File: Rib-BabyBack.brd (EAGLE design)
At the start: 67.3 x 74.9 mm, 30 parts, among them IC1 REG1117, SW1 DPDT

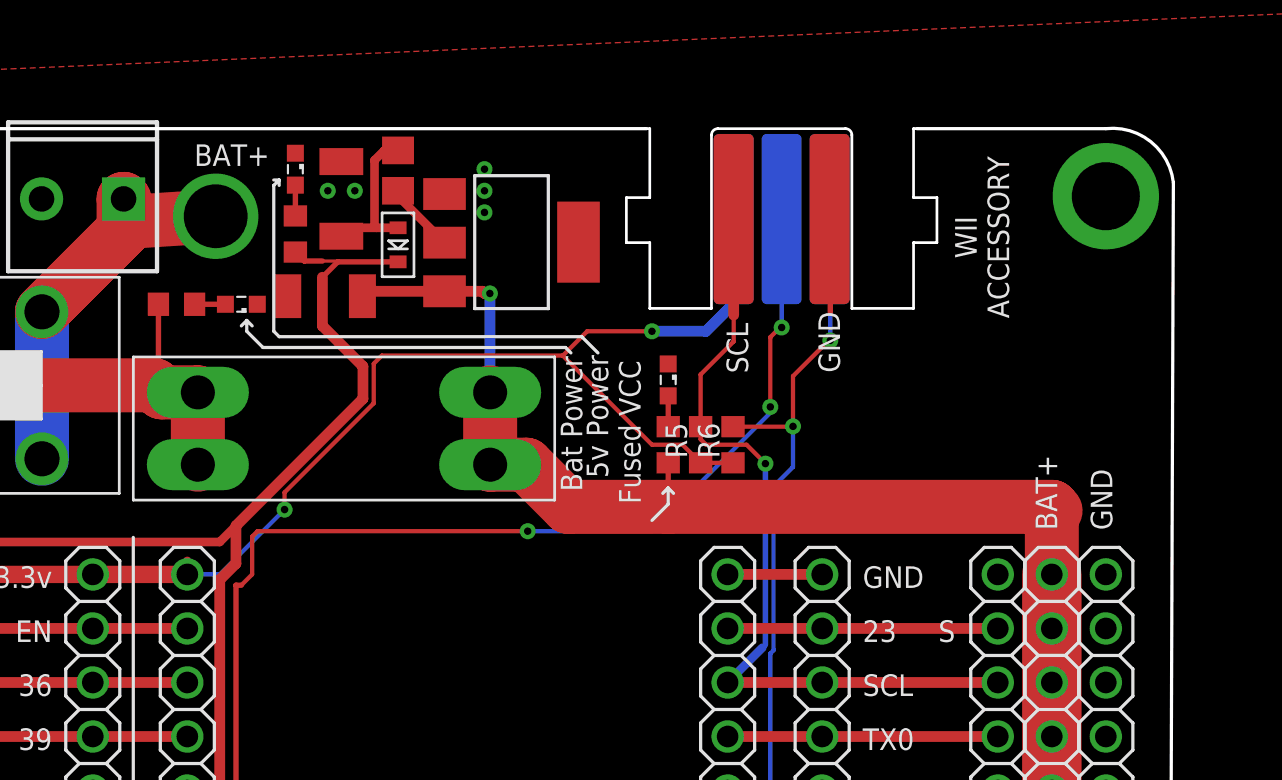
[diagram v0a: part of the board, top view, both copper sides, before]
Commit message: Moved fuse holder as per #40
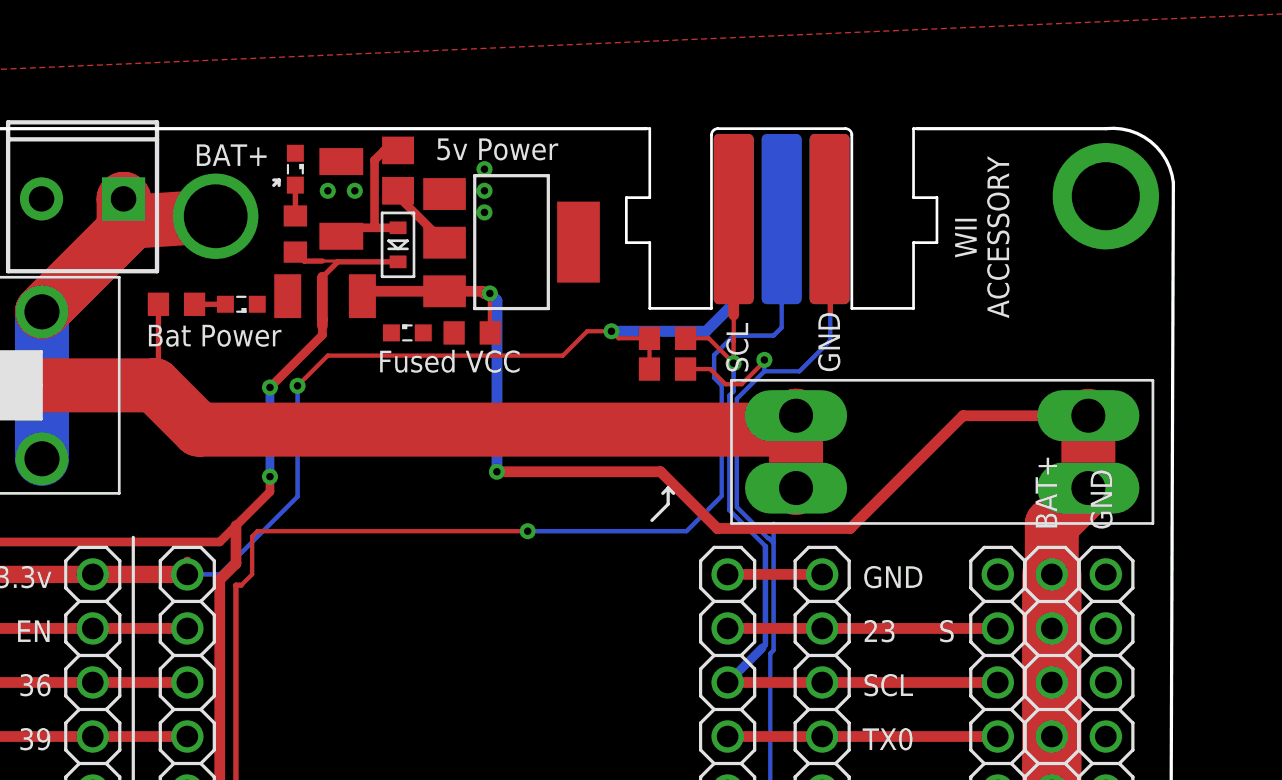
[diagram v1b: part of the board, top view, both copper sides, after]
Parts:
- moved F4 28.1 mm to (56.8, 60.4)
- moved LED1 12.5 mm to (31.7, 66.0), turned to 0 degrees
- moved R1 10.6 mm to (34.7, 66.0), turned to 0 degrees
- moved R5 5.24 mm to (43.9, 65.7), turned to 0 degrees
- moved R6 4.70 mm to (43.9, 64.3), turned to 0 degrees
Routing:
- net LIPORAW: track 35.5 -> 64.6 mm
- net VCC: track 139.9 -> 147.5 mm, vias 1 -> 2
- net SDA: track 45.6 -> 51.1 mm, vias 3 -> 2
- net 3V3: track 135.2 -> 130.0 mm
- net DET: track 77.1 -> 79.4 mm, vias 4 -> 2
- net N$24: track 1.45 -> 0.00 mm
- net 5V: track 117.4 -> 116.1 mm, vias 2 -> 4
- net SCL: track 34.2 -> 34.7 mm

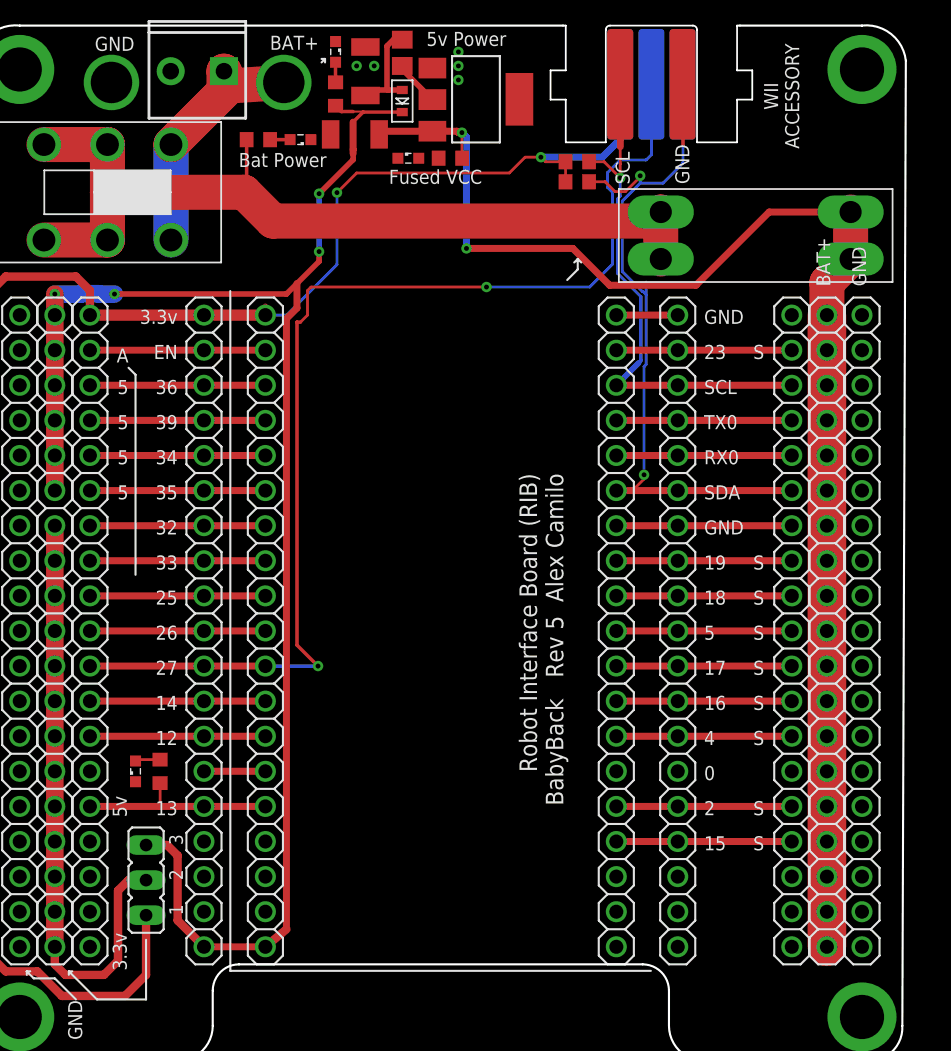
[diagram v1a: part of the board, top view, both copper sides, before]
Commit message: Updated silkscreen indicating analog pins #41
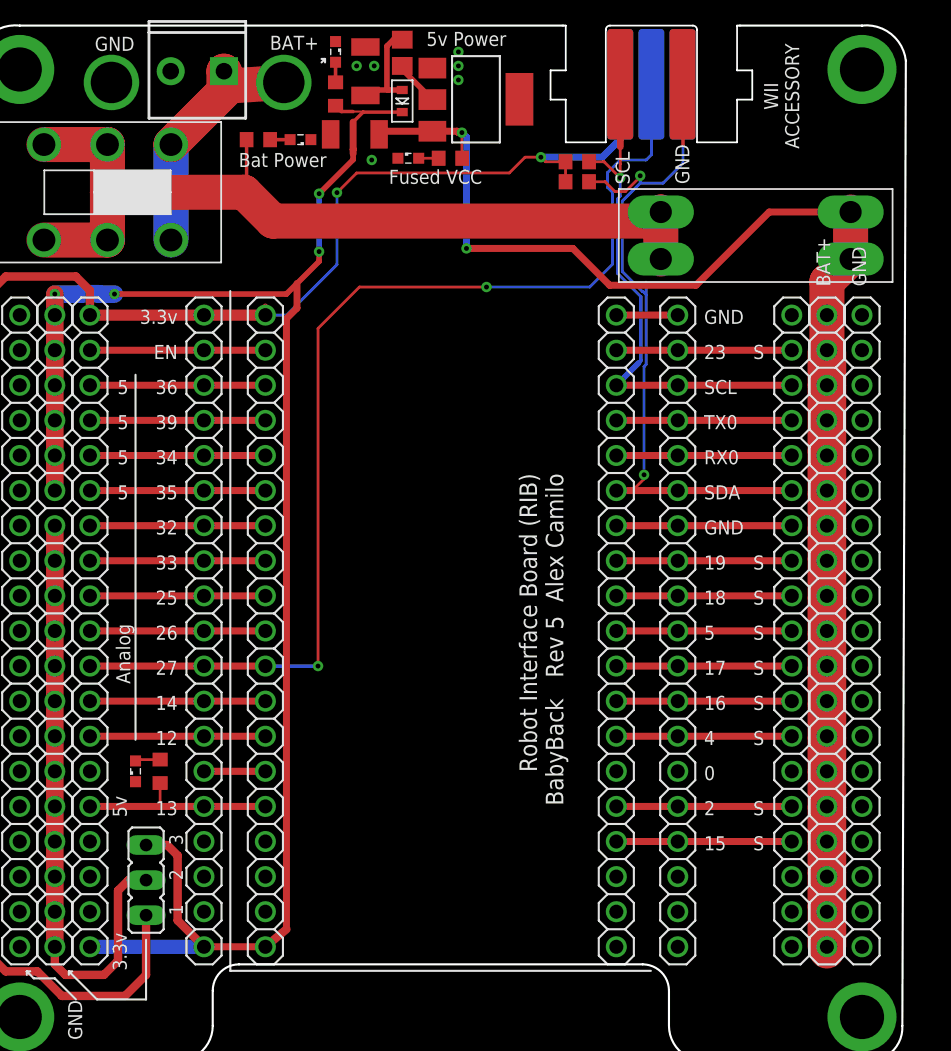
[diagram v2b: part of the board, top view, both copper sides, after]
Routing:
- net 5V: track 116.1 -> 124.4 mm
- net SDA: track 51.1 -> 55.0 mm
- net N$24: track 0.00 -> 1.45 mm
- net VCC: track 147.5 -> 146.1 mm
- net DET: track 79.4 -> 80.1 mm
- net GND: vias 10 -> 11
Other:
- board text added: "Analog"
- board text removed: "A"

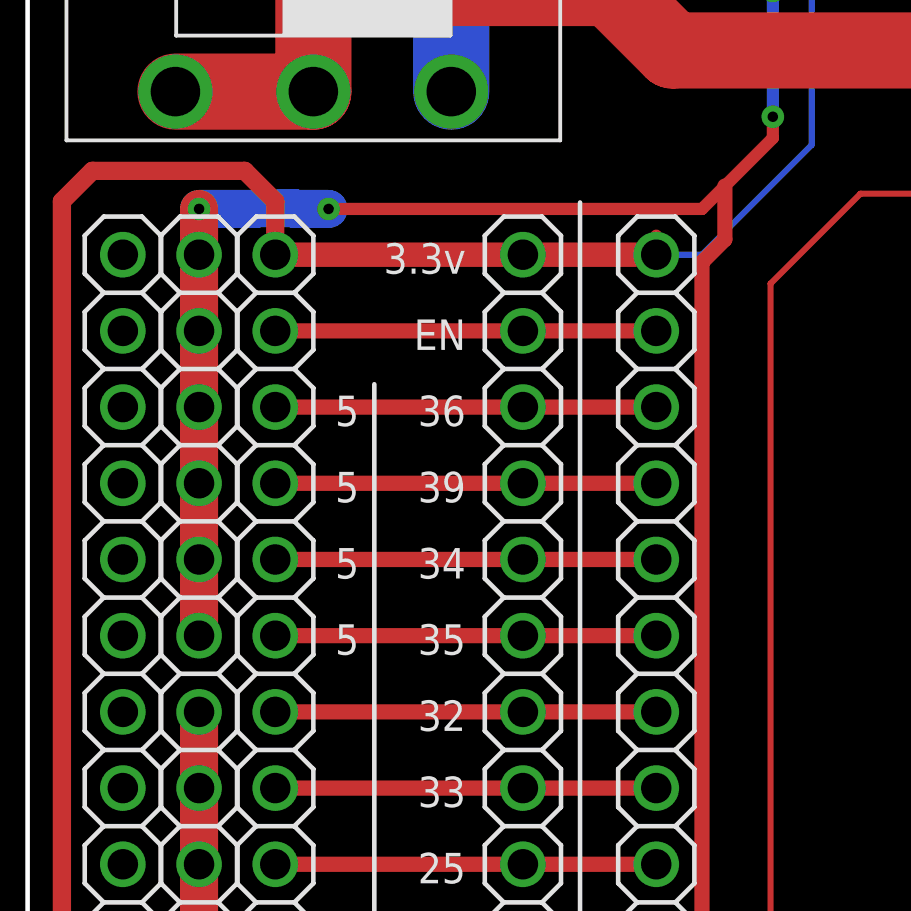
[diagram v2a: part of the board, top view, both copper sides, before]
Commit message: changed 5v rail
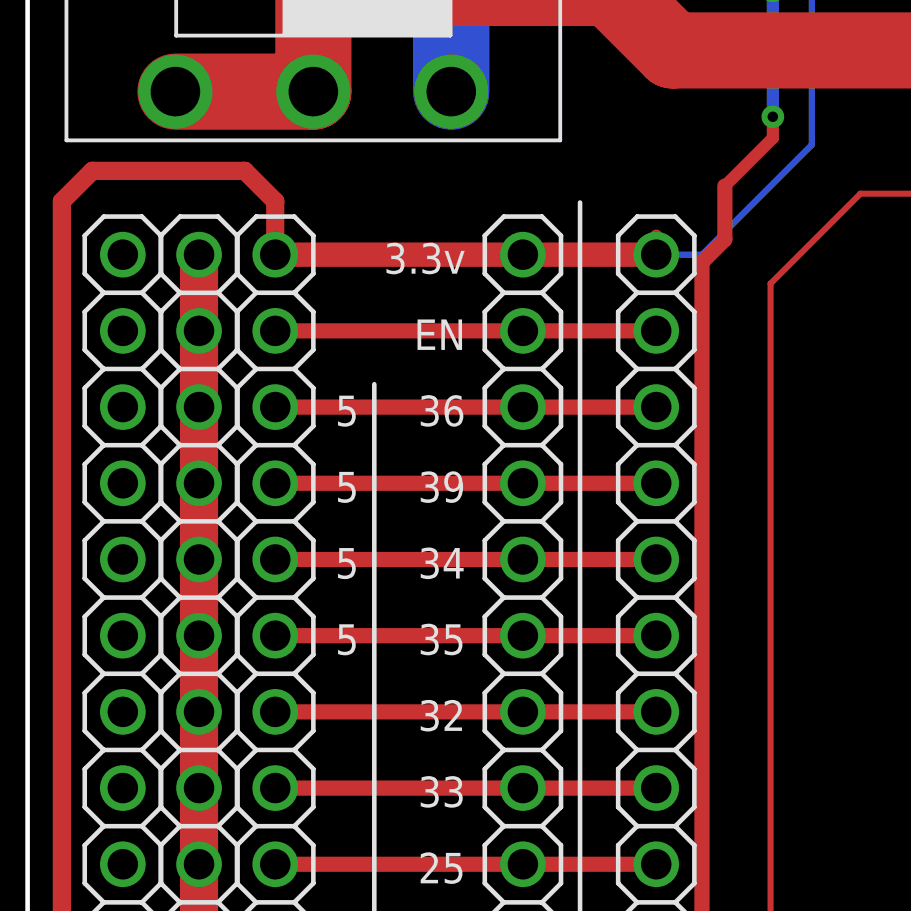
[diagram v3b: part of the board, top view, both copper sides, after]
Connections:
- net 5V: no longer JP4.14, JP4.15, JP4.16, JP4.17, JP4.18, JP4.19
- net SENSORV: now also JP4.14, JP4.15, JP4.16, JP4.17, JP4.18, JP4.19
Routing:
- net 5V: track 124.4 -> 92.3 mm, vias 4 -> 2
- net SENSORV: track 44.5 -> 59.7 mm
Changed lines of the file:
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@@
 <?xml version="1.0" encoding="utf-8"?>
 <!DOCTYPE eagle SYSTEM "eagle.dtd">
-<eagle version="8.6.3">
+<eagle version="9.1.0">
 <drawing>
 <settings>
@@
 <param name="checkStop" value="0"/>
 <param name="checkValues" value="0"/>
+<param name="checkNames" value="1"/>
+<param name="checkWireStubs" value="1"/>
+<param name="checkPolygonWidth" value="0"/>
 <param name="useDiameter" value="13"/>
 <param name="maxErrors" value="50"/>
@@
 <wire x1="31.242" y1="69.304" x2="28.41" y2="69.304" width="0.254" layer="1"/>
 <wire x1="28.41" y1="69.304" x2="27.686" y2="68.58" width="0.254" layer="1"/>
-<contactref element="JP4" pad="15"/>
-<contactref element="JP4" pad="19"/>
-<contactref element="JP4" pad="16"/>
-<contactref element="JP4" pad="17"/>
-<contactref element="JP4" pad="18"/>
-<contactref element="JP4" pad="14"/>
-<wire x1="6.096" y1="41.91" x2="6.096" y2="44.45" width="1.27" layer="1"/>
-<wire x1="6.096" y1="44.45" x2="6.096" y2="46.99" width="1.27" layer="1"/>
-<wire x1="6.096" y1="46.99" x2="6.096" y2="49.53" width="1.27" layer="1"/>
-<wire x1="6.096" y1="49.53" x2="6.096" y2="52.07" width="1.27" layer="1"/>
-<wire x1="6.096" y1="52.07" x2="6.096" y2="54.61" width="1.27" layer="1"/>
-<wire x1="6.096" y1="54.61" x2="6.096" y2="56.134" width="1.27" layer="1"/>
-<via x="6.096" y="56.134" extent="1-16" drill="0.35"/>
-<via x="10.414" y="56.134" extent="1-16" drill="0.35"/>
-<wire x1="6.096" y1="56.134" x2="7.9688125" y2="56.134" width="1.27" layer="16"/>
-<wire x1="7.9688125" y1="56.134" x2="7.9942125" y2="56.1594" width="1.27" layer="16"/>
-<wire x1="7.9942125" y1="56.1594" x2="9.2777875" y2="56.1594" width="1.27" layer="16"/>
-<wire x1="9.2777875" y1="56.1594" x2="9.3031875" y2="56.134" width="1.27" layer="16"/>
-<wire x1="9.3031875" y1="56.134" x2="10.414" y2="56.134" width="1.27" layer="16"/>
-<wire x1="10.414" y1="56.134" x2="22.86" y2="56.134" width="0.4064" layer="1"/>
-<wire x1="22.86" y1="56.134" x2="23.622" y2="56.896" width="0.4064" layer="1"/>
 <wire x1="28.41" y1="69.304" x2="28.372" y2="69.342" width="0.1524" layer="1"/>
 <wire x1="28.372" y1="69.342" x2="26.836" y2="69.342" width="0.1524" layer="1"/>
@@
 <wire x1="6.096" y1="34.29" x2="6.096" y2="36.83" width="1.27" layer="1"/>
 <wire x1="6.096" y1="36.83" x2="6.096" y2="39.37" width="1.27" layer="1"/>
+<contactref element="JP4" pad="15"/>
+<contactref element="JP4" pad="19"/>
+<contactref element="JP4" pad="16"/>
+<contactref element="JP4" pad="17"/>
+<contactref element="JP4" pad="18"/>
+<contactref element="JP4" pad="14"/>
+<wire x1="6.096" y1="44.45" x2="6.096" y2="46.99" width="1.27" layer="1"/>
+<wire x1="6.096" y1="46.99" x2="6.096" y2="49.53" width="1.27" layer="1"/>
+<wire x1="6.096" y1="49.53" x2="6.096" y2="52.07" width="1.27" layer="1"/>
+<wire x1="6.096" y1="52.07" x2="6.096" y2="54.61" width="1.27" layer="1"/>
+<wire x1="6.096" y1="44.45" x2="6.096" y2="41.91" width="1.27" layer="1"/>
+<wire x1="6.096" y1="41.91" x2="6.096" y2="39.37" width="1.27" layer="1"/>
 </signal>
 <signal name="N$6">
@@
 </signal>
 </signals>
+<mfgpreviewcolors>
+<mfgpreviewcolor name="soldermaskcolor" color="0xC8008000"/>
+<mfgpreviewcolor name="silkscreencolor" color="0xFFFEFEFE"/>
+<mfgpreviewcolor name="backgroundcolor" color="0xFF282828"/>
+<mfgpreviewcolor name="coppercolor" color="0xFFFFBF00"/>
+<mfgpreviewcolor name="substratecolor" color="0xFF786E46"/>
+</mfgpreviewcolors>
 </board>
 </drawing>
